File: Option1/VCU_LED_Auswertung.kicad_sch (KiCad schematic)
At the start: 3 parts

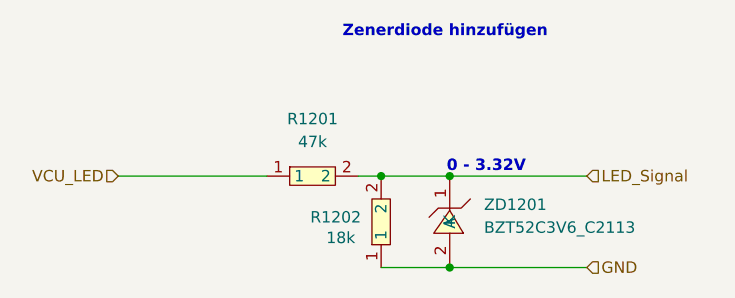
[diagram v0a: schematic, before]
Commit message: SPI Flash hinzugefügt, IN/Outputs vereinheitlicht, USB Flash Möglichkeit hinzugefügt, Display fehtl noch
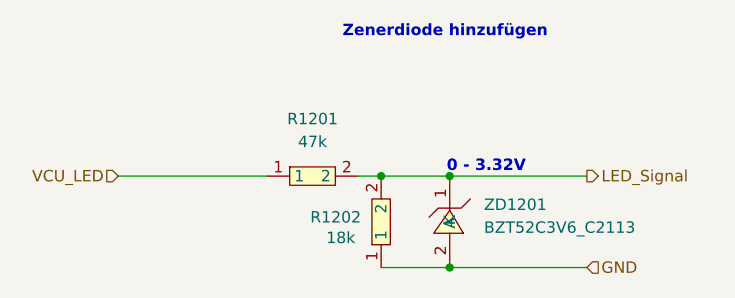
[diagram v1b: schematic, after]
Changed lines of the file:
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@@
 (kicad_sch
-	(version 20231120)
+	(version 20250114)
 	(generator "eeschema")
-	(generator_version "8.0")
+	(generator_version "9.0")
 	(paper "A4")
 	(title_block
@@
 		(comment 2 "Bachelorarbiet")
 		(comment 3 "Sebastian Hampl")
+	)
+	(text "0 - 3.32V"
+		(exclude_from_sim no)
+		(at 117.094 65.024 0)
+		(effects
+			(font
+				(size 1.27 1.27)
+				(thickness 0.254)
+				(bold yes)
+			)
+		)
+	)
+	(text "Zenerdiode hinzufügen\n"
+		(exclude_from_sim no)
+		(at 112.522 50.038 0)
+		(effects
+			(font
+				(size 1.27 1.27)
+				(thickness 0.254)
+				(bold yes)
+			)
+		)
 	)
 	(junction
@@
 		)
 	)
-	(text "0 - 3.32V"
-		(exclude_from_sim no)
-		(at 117.094 65.024 0)
-		(effects
-			(font
-				(size 1.27 1.27)
-				(thickness 0.254)
-				(bold yes)
-			)
-		)
-	)
-	(text "Zenerdiode hinzufügen\n"
-		(exclude_from_sim no)
-		(at 112.522 50.038 0)
-		(effects
-			(font
-				(size 1.27 1.27)
-				(thickness 0.254)
-				(bold yes)
-			)
-		)
-	)
 	(hierarchical_label "LED_Signal"
-		(shape input)
+		(shape output)
 		(at 128.27 66.04 0)
 		(effects

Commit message: Added Export for Review 1
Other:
- note removed: "Zenerdiode hinzufügen"
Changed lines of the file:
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@@
-		)
-	)
-	(text "Zenerdiode hinzufügen\n"
-		(exclude_from_sim no)
-		(at 112.522 50.038 0)
-		(effects
-			(font
-				(size 1.27 1.27)
-				(thickness 0.254)
-				(bold yes)
-			)
 		)
 	)

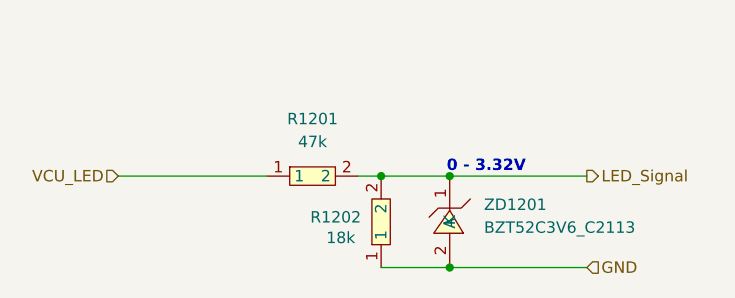
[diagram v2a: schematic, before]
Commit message: Widerstandswerte des  Spannungsteiler angepasst und korrigiert
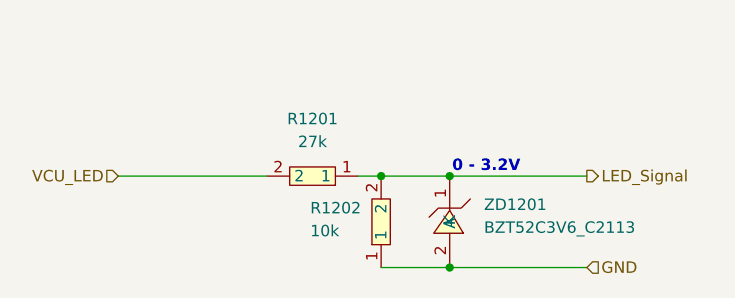
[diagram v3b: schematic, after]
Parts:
- removed R1201: 47k, easyeda2kicad:R0603, symbol easyeda2kicad:0603WAF4702T5E
- removed R1202: 18k, easyeda2kicad:R0603, symbol easyeda2kicad:0603WAF1802T5E
- added R1201: 27k, easyeda2kicad:R0603, symbol EasyEda2KiCad:0603WAF2702T5E
- added R1202: 10k, easyeda2kicad:R0603, symbol EasyEda2KiCad:0603WAF1002T5E
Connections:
- net GND: now also R1202.1
- net LED_Signal: now also R1201.1, R1202.2
- net VCU_LED: now also R1201.2
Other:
- note added: "0 - 3.2V"
- note removed: "0 - 3.32V"
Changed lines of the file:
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@@
 		(comment 3 "Sebastian Hampl")
 	)
-	(text "0 - 3.32V"
+	(text "0 - 3.2V"
 		(exclude_from_sim no)
 		(at 117.094 65.024 0)
@@
 	)
 	(symbol
-		(lib_id "easyeda2kicad:0603WAF4702T5E")
-		(at 97.79 66.04 0)
+		(lib_id "EasyEda2KiCad:0603WAF2702T5E")
+		(at 97.79 66.04 180)
 		(unit 1)
 		(exclude_from_sim no)
@@
 			)
 		)
-		(property "Value" "47k"
+		(property "Value" "27k"
 			(at 97.79 62.23 0)
 			(effects
@@
 		)
 		(property "Footprint" "easyeda2kicad:R0603"
-			(at 97.79 73.66 0)
-			(effects
-				(font
-					(size 1.27 1.27)
-				)
-				(hide yes)
-			)
-		)
-		(property "Datasheet" "https://lcsc.com/product-detail/Chip-Resistor-Surface-Mount-UniOhm_47KR-4702-1_C25819.html"
-			(at 97.79 76.2 0)
+			(at 97.79 58.42 0)
+			(effects
+				(font
+					(size 1.27 1.27)
+				)
+				(hide yes)
+			)
+		)
+		(property "Datasheet" "https://lcsc.com/product-detail/Chip-Resistor-Surface-Mount-UniOhm_27KR-2702-1_C22967.html"
+			(at 97.79 55.88 0)
 			(effects
 				(font
@@
 			)
 		)
-		(property "LCSC Part" "C25819"
-			(at 97.79 78.74 0)
+		(property "LCSC Part" "C22967"
+			(at 97.79 53.34 0)
 			(effects
 				(font
@@
 		)
 		(instances
-			(project "Option1"
+			(project ""
 				(path "/b9e5f262-9648-4b79-bdd1-af888b822329/3c8ea371-444a-4744-b7e3-225c455221a8"
 					(reference "R1201")
+					(unit 1)
+				)
+			)
+		)
+	)
+	(symbol
+		(lib_id "EasyEda2KiCad:0603WAF1002T5E")
+		(at 105.41 71.12 90)
+		(unit 1)
+		(exclude_from_sim no)
+		(in_bom yes)
+		(on_board yes)
+		(dnp no)
+		(property "Reference" "R1202"
+			(at 97.536 69.596 90)
+			(effects
+				(font
+					(size 1.27 1.27)
+				)
+				(justify right)
+			)
+		)
+		(property "Value" "10k"
+			(at 97.536 72.136 90)
+			(effects
+				(font
+					(size 1.27 1.27)
+				)
+				(justify right)
+			)
+		)
+		(property "Footprint" "easyeda2kicad:R0603"
+			(at 113.03 71.12 0)
+			(effects
+				(font
+					(size 1.27 1.27)
+				)
+				(hide yes)
+			)
+		)
+		(property "Datasheet" "https://lcsc.com/product-detail/Chip-Resistor-Surface-Mount-UniOhm_10KR-1002-1_C25804.html"
+			(at 115.57 71.12 0)
+			(effects
+				(font
+					(size 1.27 1.27)
+				)
+				(hide yes)
+			)
+		)
+		(property "Description" ""
+			(at 105.41 71.12 0)
+			(effects
+				(font
+					(size 1.27 1.27)
+				)
+				(hide yes)
+			)
+		)
+		(property "LCSC Part" "C25804"
+			(at 118.11 71.12 0)
+			(effects
+				(font
+					(size 1.27 1.27)
+				)
+				(hide yes)
+			)
+		)
+		(pin "2"
+		)
+		(pin "1"
+		)
+		(instances
+			(project ""
+				(path "/b9e5f262-9648-4b79-bdd1-af888b822329/3c8ea371-444a-4744-b7e3-225c455221a8"
+					(reference "R1202")
 					(unit 1)
 				)
@@
 					(unit 1)
 				)
-			)
-		)
-	)
-	(symbol
-		(lib_id "easyeda2kicad:0603WAF1802T5E")
-		(at 105.41 71.12 90)
-		(unit 1)
-		(exclude_from_sim no)
-		(in_bom yes)
-		(on_board yes)
-		(dnp no)
-		(property "Reference" "R1202"
-			(at 97.536 70.612 90)
-			(effects
-				(font
-					(size 1.27 1.27)
-				)
-				(justify right)
-			)
-		)
-		(property "Value" "18k"
-			(at 99.314 72.898 90)
-			(effects
-				(font
-					(size 1.27 1.27)
-				)
-				(justify right)
-			)
-		)
-		(property "Footprint" "easyeda2kicad:R0603"
-			(at 113.03 71.12 0)
-			(effects
-				(font
-					(size 1.27 1.27)
-				)
-				(hide yes)
-			)
-		)
-		(property "Datasheet" "https://lcsc.com/product-detail/Chip-Resistor-Surface-Mount-UniOhm_18KR-1802-1_C25810.html"
-			(at 115.57 71.12 0)
-			(effects
-				(font
-					(size 1.27 1.27)
-				)
-				(hide yes)
-			)
-		)
-		(property "Description" ""
-			(at 105.41 71.12 0)
-			(effects
-				(font
-					(size 1.27 1.27)
-				)
-				(hide yes)
-			)
-		)
-		(property "LCSC Part" "C25810"
-			(at 118.11 71.12 0)
-			(effects
-				(font
-					(size 1.27 1.27)
-				)
-				(hide yes)
-			)
-		)
-		(pin "2"
-		)
-		(pin "1"
-		)
-		(instances
-			(project ""
-				(path "/b9e5f262-9648-4b79-bdd1-af888b822329/3c8ea371-444a-4744-b7e3-225c455221a8"
-					(reference "R1202")
-					(unit 1)
-				)

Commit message: Fertigfe Abschlusspräsentation
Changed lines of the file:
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@@
 	(wire
 		(pts
-			(xy 76.2 66.04) (xy 92.71 66.04)
+			(xy 88.9 66.04) (xy 92.71 66.04)
 		)
 		(stroke
@@
 	(hierarchical_label "VCU_LED"
 		(shape input)
-		(at 76.2 66.04 180)
+		(at 88.9 66.04 180)
 		(effects
 			(font
